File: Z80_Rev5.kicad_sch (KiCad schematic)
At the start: 25 parts, among them J2 UART, J3 I2C, J5 MicroSD, J7 USB_B_Mini, SW1 ON|OFF, SW2 Z80_RESET, SW3 CUSTOM, U1 Z84C00/PLCC, U3 AS6C4008-55PCN, U4 STC8H8K64U-45I-PDIP40, U5 SST39SF040

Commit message: add sch + silk images.
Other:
- title: Z80_Rev4 -> Z80_Rev5
- moved on the sheet: C4, C5, C6, C7, C8, C9, J2, J3, J5, J7, R1, R2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

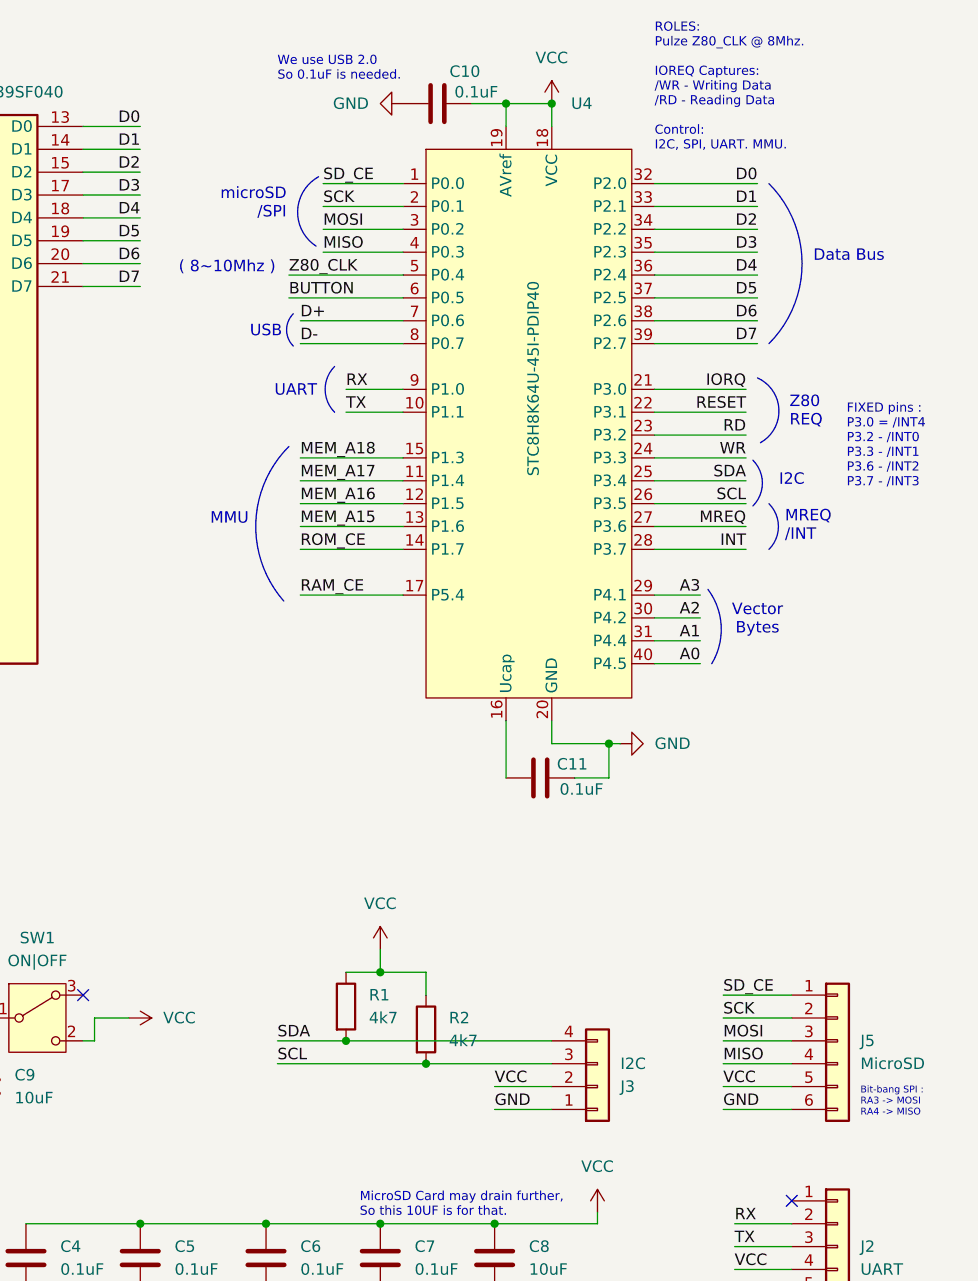
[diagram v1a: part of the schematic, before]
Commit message: refine STC8 pinmap.
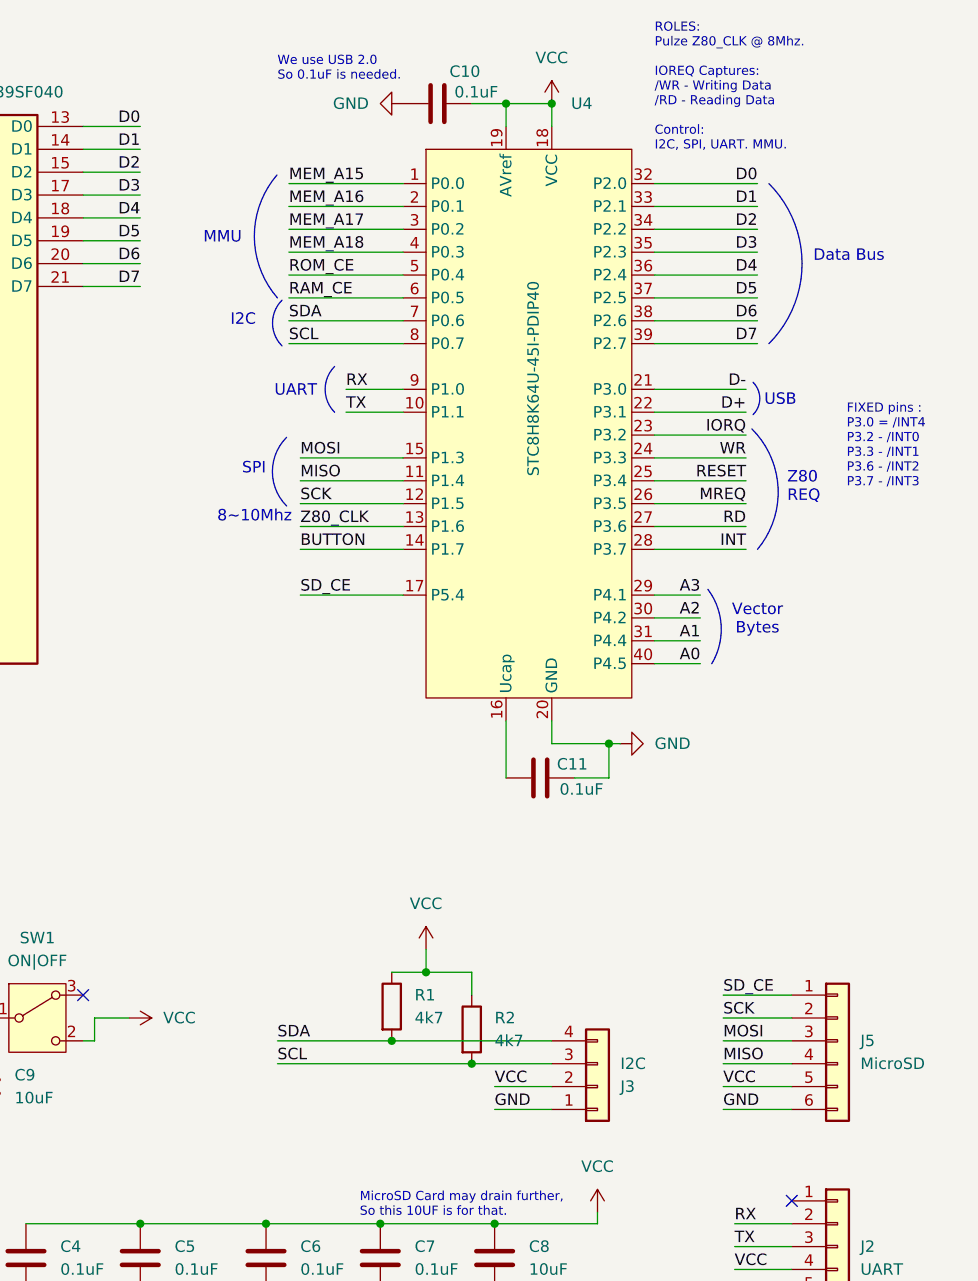
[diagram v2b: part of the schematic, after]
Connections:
- net BUTTON: now also U4.14 (P1.7); no longer U4.6 (P0.5)
- net D+: now also U4.22 (P3.1); no longer U4.7 (P0.6)
- net D-: now also U4.21 (P3.0); no longer U4.8 (P0.7)
- net IORQ: now also U4.23 (P3.2); no longer U4.21 (P3.0)
- net MEM_A15: now also U4.1 (P0.0); no longer U4.13 (P1.6)
- net MEM_A16: now also U4.2 (P0.1); no longer U4.12 (P1.5)
- net MEM_A17: now also U4.3 (P0.2); no longer U4.11 (P1.4)
- net MEM_A18: now also U4.4 (P0.3); no longer U4.15 (P1.3)
- net MISO: now also U4.11 (P1.4); no longer U4.4 (P0.3)
- net MOSI: now also U4.15 (P1.3); no longer U4.3 (P0.2)
- net MREQ: now also U4.26 (P3.5); no longer U4.27 (P3.6)
- net RAM_CE: now also U4.6 (P0.5); no longer U4.17 (P5.4)
- net RD: now also U4.27 (P3.6); no longer U4.23 (P3.2)
- net RESET: now also U4.25 (P3.4); no longer U4.22 (P3.1)
- net ROM_CE: now also U4.5 (P0.4); no longer U4.14 (P1.7)
- net SCK: now also U4.12 (P1.5); no longer U4.2 (P0.1)
- net SCL: now also U4.8 (P0.7); no longer U4.26 (P3.5)
- net SDA: now also U4.7 (P0.6); no longer U4.25 (P3.4)
- net SD_CE: now also U4.17 (P5.4); no longer U4.1 (P0.0)
- net Z80_CLK: now also U4.13 (P1.6); no longer U4.5 (P0.4)
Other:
- note added: "8~10Mhz"
- note added: "SPI"
- note removed: "( 8~10Mhz )"
- note removed: "Bit-bang SPI : RA3 -> MOSI RA4 -> MISO"
- note removed: "MREQ /INT"
- note removed: "microSD /SPI"
- moved on the sheet: R1, R2

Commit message: Remove C4 because too many of them.
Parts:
- removed C4: 0.1uF, Capacitor_THT:C_Disc_D3.4mm_W2.1mm_P2.50mm, symbol Device:C
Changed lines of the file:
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@@
 	)
 	(junction
-		(at 193.04 148.59)
-		(diameter 0)
-		(color 0 0 0 0)
-	)
-	(junction
 		(at 156.21 140.97)
 		(diameter 0)
@@
 	)
 	(junction
-		(at 193.04 156.21)
-		(diameter 0)
-		(color 0 0 0 0)
-	)
-	(junction
-		(at 238.76 24.13)
-		(diameter 0)
-		(color 0 0 0 0)
-	)
-	(junction
 		(at 229.87 130.81)
 		(diameter 0)
@@
 	)
 	(junction
+		(at 238.76 24.13)
+		(diameter 0)
+		(color 0 0 0 0)
+	)
+	(junction
 		(at 245.11 95.25)
 		(diameter 0)
@@
 	(wire
 		(pts
-			(xy 180.34 148.59) (xy 193.04 148.59)
-		)
-		(stroke
-			(width 0)
-			(type default)
-		)
-	)
-	(wire
-		(pts
 			(xy 13.97 127) (xy 26.67 127)
 		)
@@
 	(wire
 		(pts
+			(xy 238.76 21.59) (xy 238.76 24.13)
+		)
+		(stroke
+			(width 0)
+			(type default)
+		)
+	)
+	(wire
+		(pts
 			(xy 130.81 40.64) (xy 124.46 40.64)
 		)
@@
 	(wire
 		(pts
-			(xy 180.34 156.21) (xy 193.04 156.21)
-		)
-		(stroke
-			(width 0)
-			(type default)
-		)
-	)
-	(wire
-		(pts
 			(xy 133.35 58.42) (xy 124.46 58.42)
 		)
@@
 	(symbol
 		(lib_id "power:VCC")
-		(at 238.76 24.13 0)
+		(at 238.76 21.59 0)
 		(unit 1)
 		(body_style 1)
@@
 		(fields_autoplaced yes)
 		(property "Reference" "#PWR014"
-			(at 238.76 27.94 0)
+			(at 238.76 25.4 0)
 			(hide yes)
 			(show_name no)
@@
 		)
 		(property "Value" "VCC"
-			(at 238.76 19.05 0)
+			(at 238.76 16.51 0)
 			(show_name no)
 			(do_not_autoplace no)
@@
 		)
 		(property "Footprint" ""
-			(at 238.76 24.13 0)
+			(at 238.76 21.59 0)
 			(hide yes)
 			(show_name no)
@@
 		)
 		(property "Datasheet" ""
-			(at 238.76 24.13 0)
+			(at 238.76 21.59 0)
 			(hide yes)
 			(show_name no)
@@
 		)
 		(property "Description" "Power symbol creates a global label with name \"VCC\""
-			(at 238.76 24.13 0)
+			(at 238.76 21.59 0)
 			(hide yes)
 			(show_name no)
@@
 					(unit 1)
 				)
-			)
-		)
-	)
-	(symbol
-		(lib_id "Device:C")
-		(at 180.34 152.4 180)
-		(unit 1)
-		(body_style 1)
-		(exclude_from_sim no)
-		(in_bom yes)
-		(on_board yes)
-		(in_pos_files yes)
-		(dnp no)
-		(fields_autoplaced yes)
-		(property "Reference" "C4"
-			(at 184.15 151.1299 0)
-			(show_name no)
-			(do_not_autoplace no)
-			(effects
-				(font
-					(size 1.27 1.27)
-				)
-				(justify right)
-			)
-		)
-		(property "Value" "0.1uF"
-			(at 184.15 153.6699 0)
-			(show_name no)
-			(do_not_autoplace no)
-			(effects
-				(font
-					(size 1.27 1.27)
-				)
-				(justify right)
-			)
-		)
-		(property "Footprint" "Capacitor_THT:C_Disc_D3.4mm_W2.1mm_P2.50mm"
-			(at 179.3748 148.59 0)
-			(hide yes)
-			(show_name no)
-			(do_not_autoplace no)
-			(effects
-				(font
-					(size 1.27 1.27)
-				)
-			)
-		)
-		(property "Datasheet" ""
-			(at 180.34 152.4 0)
-			(hide yes)
-			(show_name no)
-			(do_not_autoplace no)
-			(effects
-				(font
-					(size 1.27 1.27)
-				)
-			)
-		)
-		(property "Description" "Unpolarized capacitor"
-			(at 180.34 152.4 0)
-			(hide yes)
-			(show_name no)
-			(do_not_autoplace no)
-			(effects
-				(font
-					(size 1.27 1.27)
-				)
-			)
-		)
-		(pin "1"
-		)
-		(pin "2"
-		)
-		(instances
-			(project "Z80_Rev5"
-				(path "/1dee2e6f-8929-455d-a1de-5fd790cf69ac"
-					(reference "C4")
-					(unit 1)
-				)
